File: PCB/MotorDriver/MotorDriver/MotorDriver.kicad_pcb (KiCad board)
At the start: 2 copper layers, 101.3 x 73.7 mm, 92 parts, among them J1 XT30PW-M, J10 JST-XH, J11 JST-XH, J12 JST-XH, J13 JST-XH, J14 JST-XH, J15 JST-XH, J16 JST-XH, J17 JST-XH, J18 JST-XH, J19 JST-XH, J2 JST-XH, J20 JST-XH, J21 JST-XH, J22 JST-XH, J23 JST-XH, J24 JST-XH, J3 XT30PW-M, J4 XT30PW-M, J5 JST-XH, J6 JST-XH, J7 JST-XH, J8 JST-XH, J9 JST-XH, Q1 TJ60S04M3L, Q10 NMOS, Q2 NMOS, Q3 NMOS, Q4 NMOS, Q5 NMOS, Q6 NMOS, Q7 NMOS, Q8 NMOS, Q9 NMOS, SW1 SW_DPST_x2, SW2 SW_Push, SW3 SW_Push, U1 DRV8701ERGET, U2 DRV8701ERGET, U3 TCA9548APWR, U4 Pico, U5 AZ1117CH-3.3TR

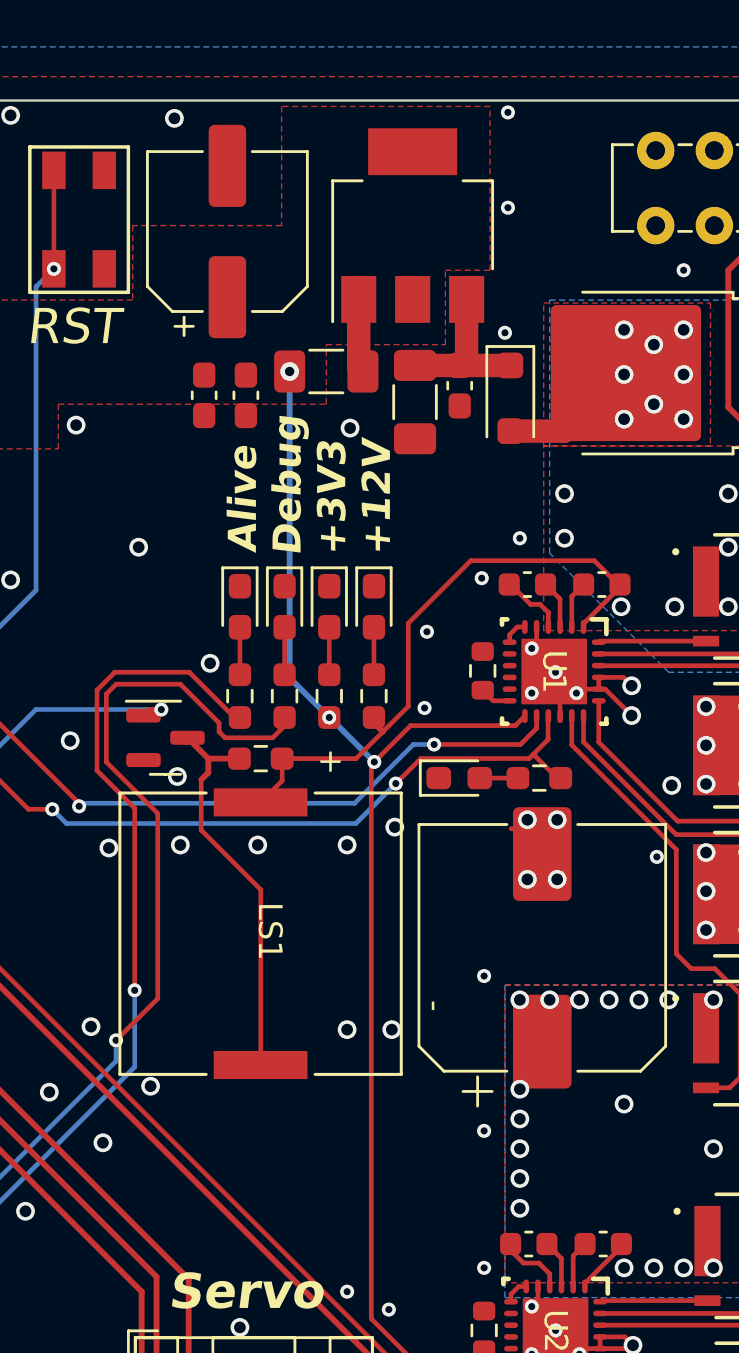
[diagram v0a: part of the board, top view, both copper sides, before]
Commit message: ✨基板をサージに強くした
- TVSをサージ発生源に近くした
- 12Vツェナーダイオードをレギュレータの近くに取り付けた
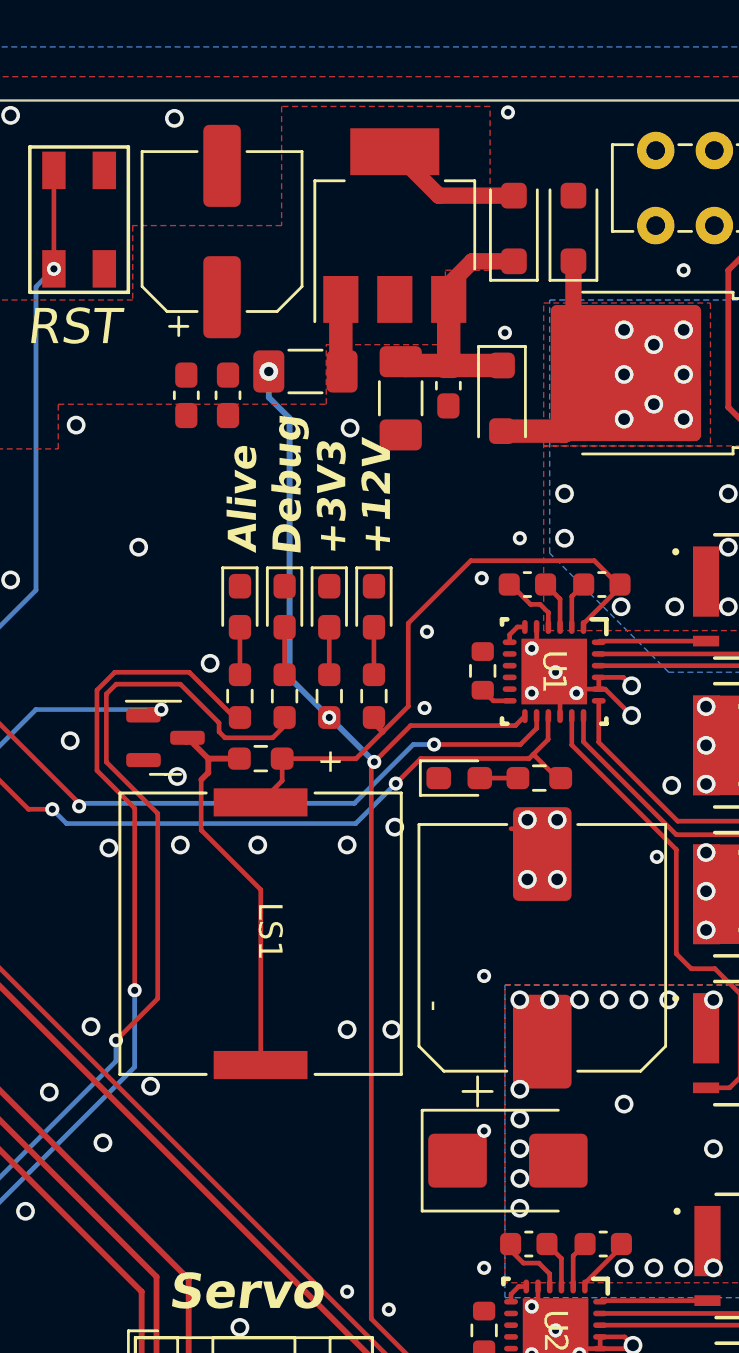
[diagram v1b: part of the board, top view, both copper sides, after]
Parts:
- added D10: ＧＳ１０１０ＦＬ, Diode_SMD:D_SOD-123F, F.Cu at (121.7, 104.3)
- added D2: ＧＳ１０１０ＦＬ, Diode_SMD:D_SOD-123F, F.Cu at (124.2, 104.3)
- added TVS1: 12V, Diode_SMD:D_SMB, F.Cu at (121.4, 144.0)
- D3: value D_Schottky -> 3.3V
- moved C7 0.89 mm to (112.8, 110.4)
- moved C13 0.76 mm to (109.5, 111.4)
- moved C15 0.76 mm to (107.7, 111.4)
- moved U5 0.76 mm to (116.6, 104.1)
- moved C6 0.63 mm to (116.8, 111.5)
- moved C5 0.48 mm to (118.9, 111.0)
- moved D1 0.36 mm to (121.2, 111.5)
- moved C14 0.23 mm to (109.2, 104.4)
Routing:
- net +3V3: track 311.3 -> 317.5 mm
- net +12V: track 65.1 -> 70.1 mm
- net /12VIN: track 7.00 -> 11.0 mm
- net GND: vias 180 -> 179
